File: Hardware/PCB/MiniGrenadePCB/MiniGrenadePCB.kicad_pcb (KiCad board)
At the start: 2 copper layers, 44.5 x 52.1 mm, 3 parts, among them U1 DF-Player_mini, U2 WeMos_D1_mini

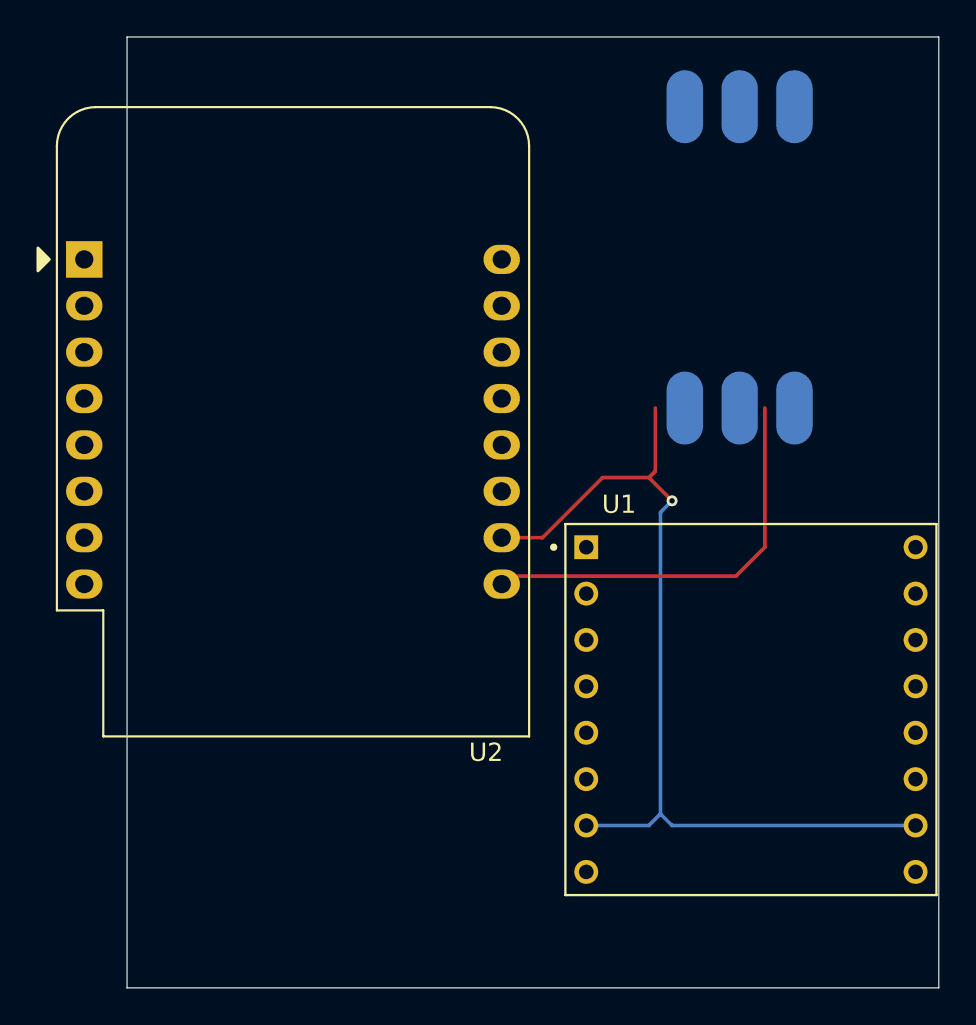
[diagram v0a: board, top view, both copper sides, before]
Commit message: Corrected PCB Oopsie+ began small grenade PCB
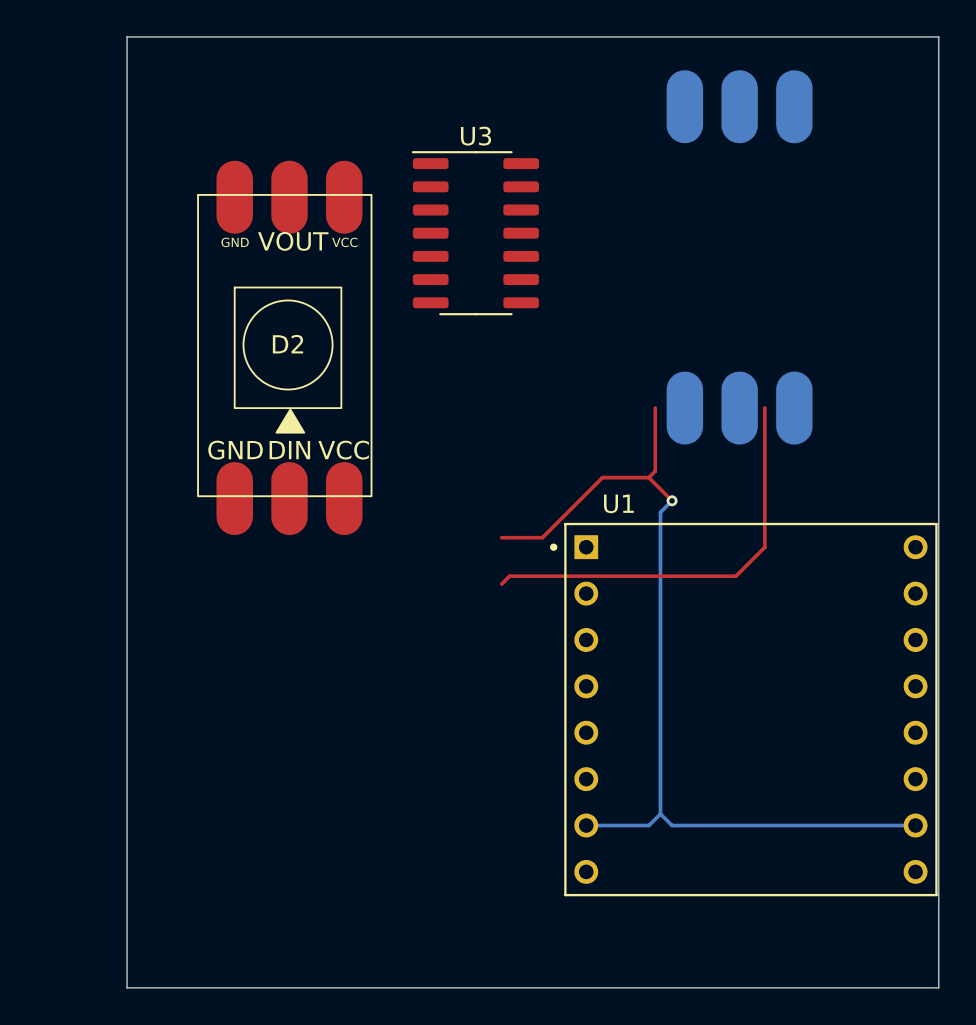
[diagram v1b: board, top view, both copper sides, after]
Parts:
- removed U2: WeMos_D1_mini, Module:WEMOS_D1_mini_light
- added D2: WS2812B Neopixel, Grenade_Stuff:NeoPixel_strip, F.Cu at (195.1, 84.3)
- added U3: ATtiny1614-SS, Package_SO:SOIC-14_3.9x8.7mm_P1.27mm, F.Cu at (204.5, 78.7)
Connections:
- net Net-(D1-GND) renamed GND
- D1 pad 1: unconnected-(D1-DIN-Pad1) -> Net-(D1-DIN)
- D1 pad 2: Net-(D1-VCC) -> +5V
- D1 pad 3: unconnected-(D1-GND1-Pad3) -> Net-(D1-GND1)
- D1 pad 4: unconnected-(D1-DOUT-Pad4) -> Net-(D1-DOUT)
- D1 pad 5: unconnected-(D1-VCC1-Pad5) -> Net-(D1-VCC1)
- U1 pad 1: unconnected-(U1-VCC-Pad1) -> +5V
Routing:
- net Net-(D1-VCC): track 22.9 -> 0.00 mm
- net (no net): track 0.00 -> 22.9 mm
